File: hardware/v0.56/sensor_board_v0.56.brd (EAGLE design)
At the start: 50.8 x 50.8 mm, 65 parts, among them J3 USB-MICROB, U1 NEOPIXEL_NANO_2427, U10 TSL2591, U11 915MHz, U12 MH-Z19, U13 CCS811-I2C, U14 IAQ-CORE-C, U15 VLP-450-F, U16 VLP-450-F, U2 FT231XQ-R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

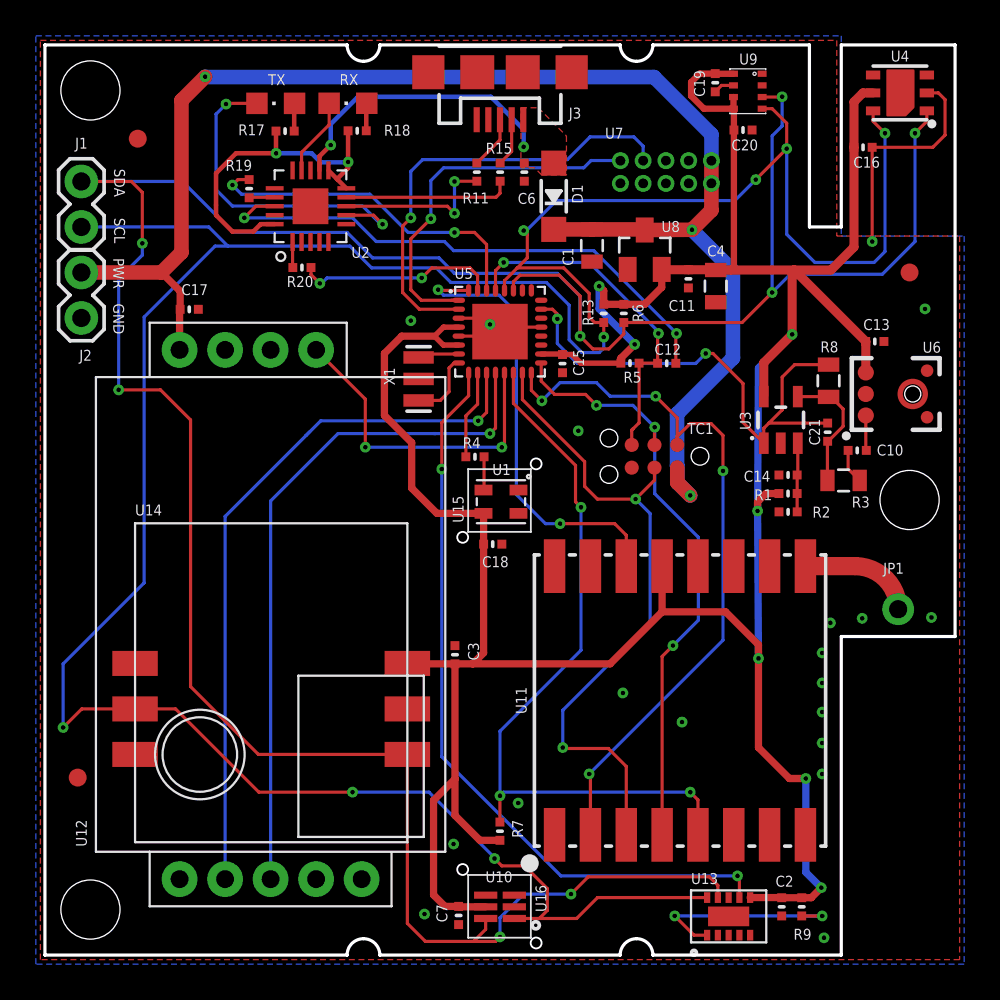
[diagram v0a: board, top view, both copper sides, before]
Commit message: Trace and silkscreen adjustments
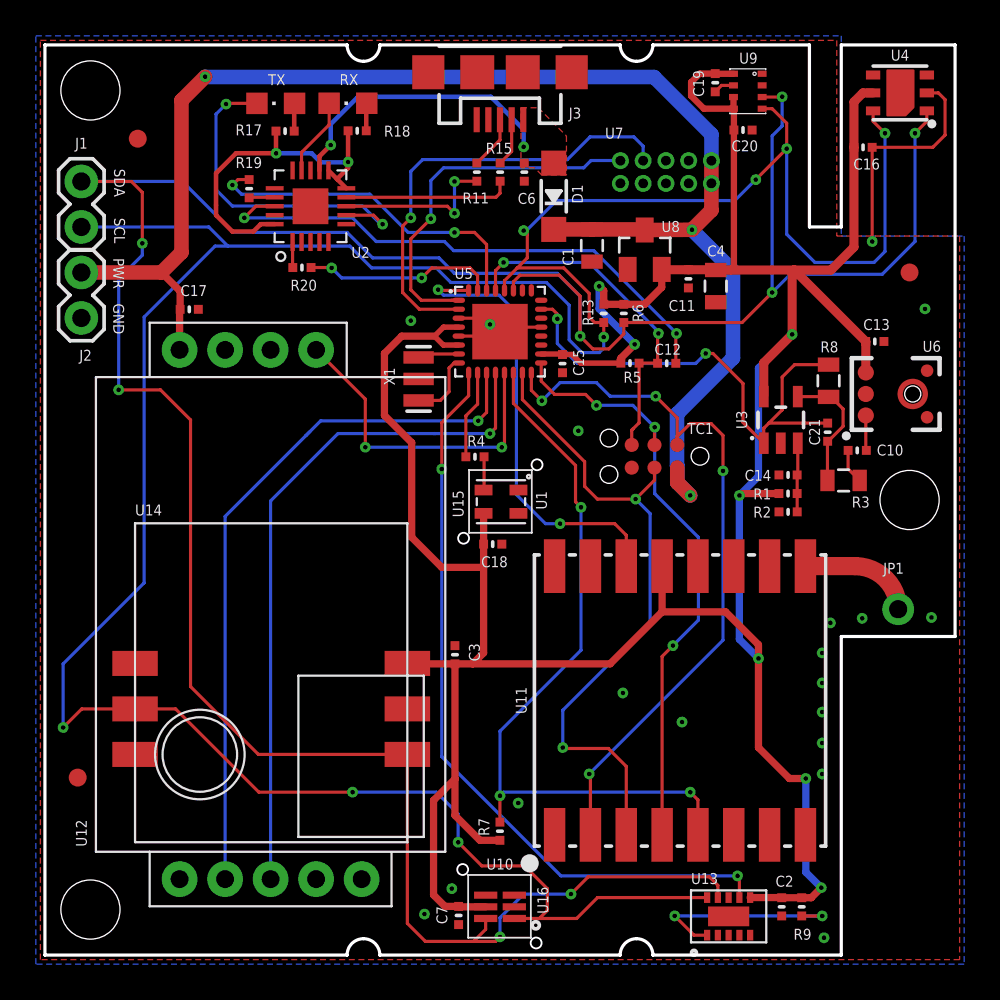
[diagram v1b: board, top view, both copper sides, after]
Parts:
- moved U15 0.07 mm to (23.4, 23.3)
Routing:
- net VCC: track 181.4 -> 185.5 mm
- net SCL: track 160.4 -> 161.4 mm
- net TX: track 11.3 -> 10.8 mm

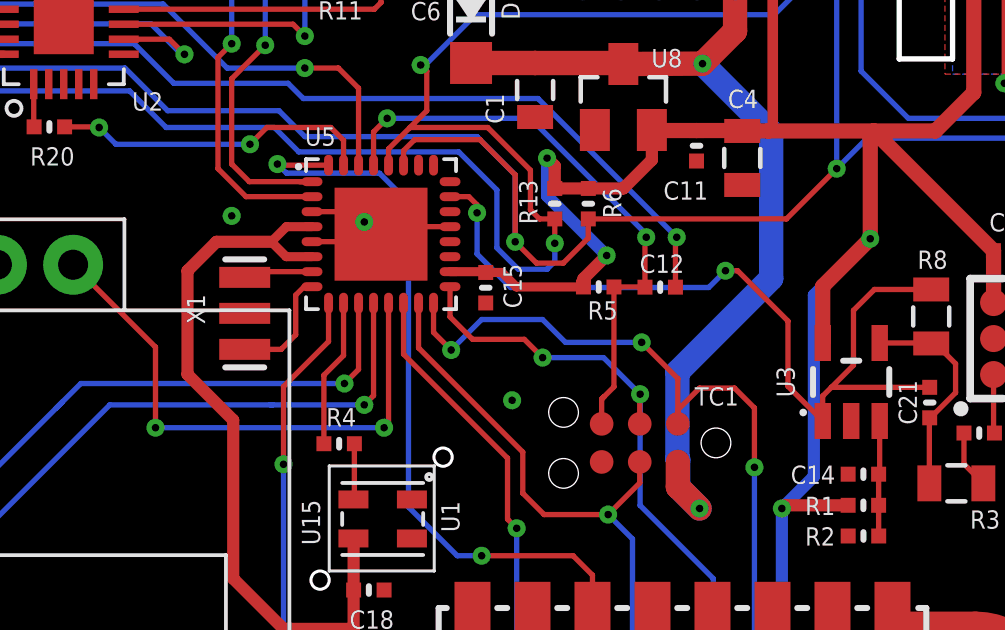
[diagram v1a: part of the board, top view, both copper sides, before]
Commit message: Added another decoupling cap to ATMega328P
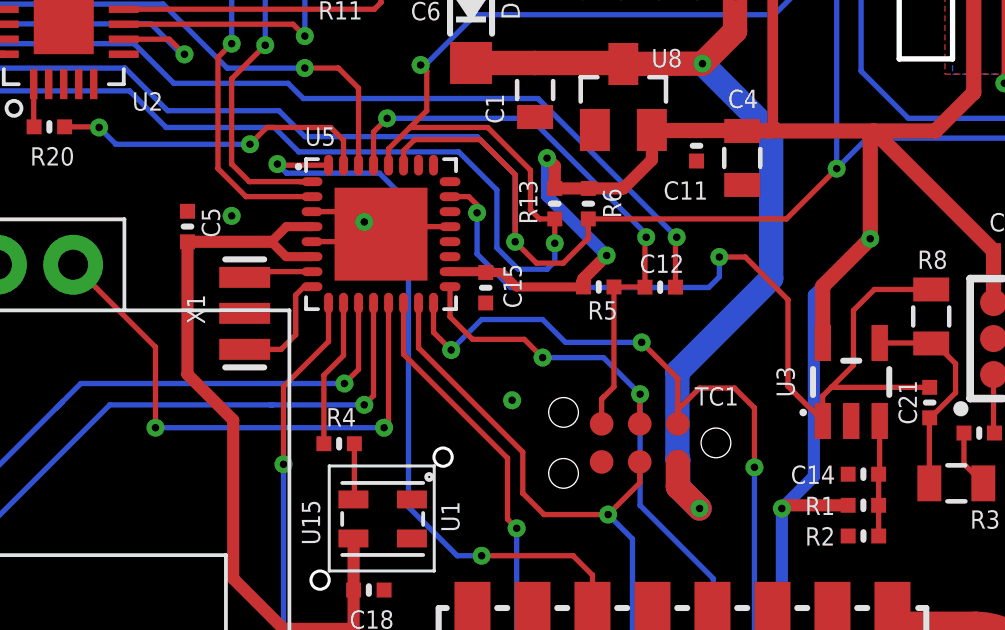
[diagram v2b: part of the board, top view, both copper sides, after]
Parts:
- added C5: 0.1uF, Adafruit Feather 32u4 Bluefruit LE:MICROBUILDER__0402MP
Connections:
- net GND: now also C5.1
- net VCC: now also C5.2
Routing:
- net A0: track 28.5 -> 29.7 mm
- net VCC: track 185.5 -> 186.1 mm
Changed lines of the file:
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@@
 <layer number="46" name="Milling" color="3" fill="1" visible="no" active="yes"/>
 <layer number="47" name="Measures" color="7" fill="1" visible="no" active="yes"/>
-<layer number="48" name="Document" color="7" fill="1" visible="no" active="yes"/>
-<layer number="49" name="Reference" color="7" fill="1" visible="no" active="yes"/>
+<layer number="48" name="Document" color="7" fill="1" visible="yes" active="yes"/>
+<layer number="49" name="Reference" color="7" fill="1" visible="yes" active="yes"/>
 <layer number="50" name="dxf" color="7" fill="1" visible="no" active="no"/>
 <layer number="51" name="tDocu" color="7" fill="1" visible="yes" active="yes"/>
@@
 <attribute name="NAME" x="27.4828" y="3.81" size="0.6096" layer="121" font="vector" rot="R270"/>
 </element>
+<element name="C5" library="Adafruit Feather 32u4 Bluefruit LE" package="MICROBUILDER__0402MP" value="0.1uF" x="18.9484" y="35.052" rot="R270"/>
 </elements>
 <signals>
@@
 <via x="43.3832" y="11.8364" extent="1-16" drill="0.25"/>
 <via x="49.1236" y="36.068" extent="1-16" drill="0.25"/>
+<contactref element="C5" pad="1"/>
 </signal>
 <signal name="VCC">
@@
 <wire x1="41.5544" y1="9.8552" x2="39.8272" y2="11.5824" width="0.4064" layer="1"/>
 <wire x1="39.8272" y1="11.5824" x2="39.8272" y2="16.5608" width="0.4064" layer="1"/>
-<wire x1="18.9484" y1="30.1244" x2="20.4724" y2="28.6004" width="0.4064" layer="1"/>
-<wire x1="18.9484" y1="30.1244" x2="18.9484" y2="33.5788" width="0.4064" layer="1"/>
-<wire x1="21.7424" y1="34.544" x2="19.9136" y2="34.544" width="0.4064" layer="1"/>
-<wire x1="18.9484" y1="33.5788" x2="19.9136" y2="34.544" width="0.4064" layer="1"/>
+<wire x1="20.4724" y1="28.6004" x2="18.9484" y2="30.1244" width="0.4064" layer="1"/>
 <wire x1="23.1" y1="35.048" x2="22.2464" y2="35.048" width="0.3048" layer="1"/>
 <wire x1="22.2464" y1="35.048" x2="21.7424" y2="34.544" width="0.3048" layer="1"/>
@@
 <wire x1="38.8662" y1="25.7598" x2="38.7604" y2="25.654" width="0.4064" layer="1"/>
 <wire x1="40.9696" y1="25.7598" x2="38.8662" y2="25.7598" width="0.4064" layer="1"/>
+<contactref element="C5" pad="2"/>
+<wire x1="18.95388125" y1="34.544" x2="18.9484" y2="34.544" width="0.4064" layer="1"/>
+<wire x1="18.95388125" y1="34.544" x2="21.7424" y2="34.544" width="0.4064" layer="1"/>
+<wire x1="18.9484" y1="34.53851875" x2="18.95388125" y2="34.544" width="0.4064" layer="1"/>
+<wire x1="18.9484" y1="30.1244" x2="18.9484" y2="34.53851875" width="0.4064" layer="1"/>
 <wire x1="24.4856" y1="22.9362" x2="24.4856" y2="21.6408" width="0" layer="19" extent="1-1"/>
 </signal>
@@
 <wire x1="28.3264" y1="36.048" x2="27.7" y2="36.048" width="0.1778" layer="1"/>
 <via x="28.6004" y="35.5092" extent="1-16" drill="0.25"/>
-<via x="36.8808" y="33.5788" extent="1-16" drill="0.25"/>
-<wire x1="38.9636" y1="31.9024" x2="38.9636" y2="29.7285" width="0.1778" layer="1"/>
-<wire x1="38.9636" y1="29.7285" x2="40.1218" y2="28.5703" width="0.1778" layer="1"/>
-<wire x1="37.2872" y1="33.5788" x2="36.8808" y2="33.5788" width="0.1778" layer="1"/>
-<wire x1="37.2872" y1="33.5788" x2="38.9636" y2="31.9024" width="0.1778" layer="1"/>
+<via x="36.6776" y="34.036" extent="1-16" drill="0.25"/>
+<wire x1="40.1218" y1="28.5703" x2="38.9636" y2="29.7285" width="0.1778" layer="1"/>
 <wire x1="43.688" y1="29.6926" x2="40.4114" y2="29.6926" width="0.1778" layer="1"/>
 <wire x1="40.1218" y1="28.5703" x2="40.1218" y2="29.403" width="0.1778" layer="1"/>
@@
 <wire x1="28.6004" y1="35.5092" x2="28.6004" y2="34.1376" width="0.1778" layer="16"/>
 <wire x1="28.6004" y1="34.1376" x2="29.718" y2="33.02" width="0.1778" layer="16"/>
-<wire x1="29.718" y1="33.02" x2="36.322" y2="33.02" width="0.1778" layer="16"/>
-<wire x1="36.322" y1="33.02" x2="36.8808" y2="33.5788" width="0.1778" layer="16"/>
+<wire x1="36.322" y1="33.02" x2="29.718" y2="33.02" width="0.1778" layer="16"/>
+<wire x1="36.6776" y1="34.036" x2="36.6776" y2="33.3756" width="0.1778" layer="16"/>
+<wire x1="36.6776" y1="33.3756" x2="36.322" y2="33.02" width="0.1778" layer="16"/>
+<wire x1="38.9636" y1="32.6136" x2="37.5412" y2="34.036" width="0.1778" layer="1"/>
+<wire x1="37.5412" y1="34.036" x2="36.6776" y2="34.036" width="0.1778" layer="1"/>
+<wire x1="38.9636" y1="29.7285" x2="38.9636" y2="32.6136" width="0.1778" layer="1"/>
 </signal>
 <signal name="DTR">

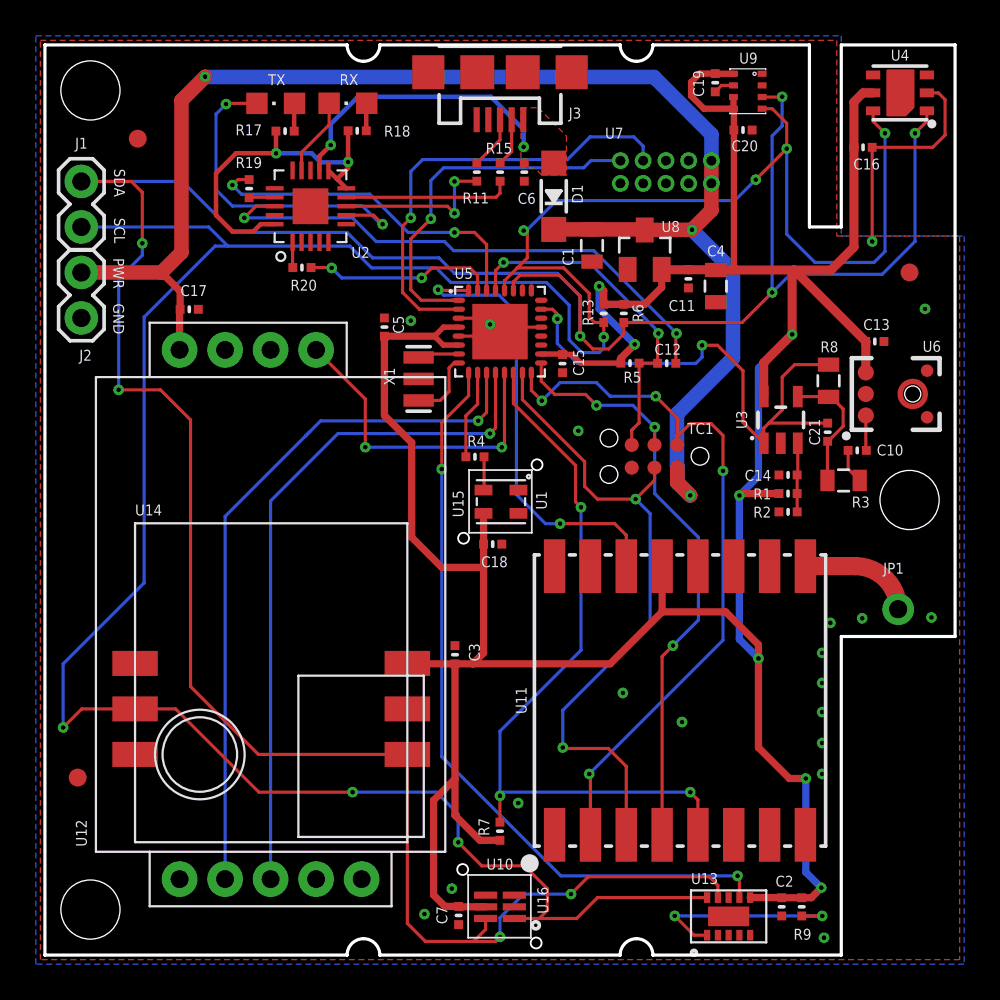
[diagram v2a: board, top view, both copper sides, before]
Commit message: v0.56b - minor adjustments
- Rerouted D9 trace to be SET pin for PM sensor instead of PWM pin for
CO2 sensor
- Added 10K pull up on D9
- Moved components away from light sensor and RGB LED's light pipe's
path
- Added extra vias all around for more ground stitching
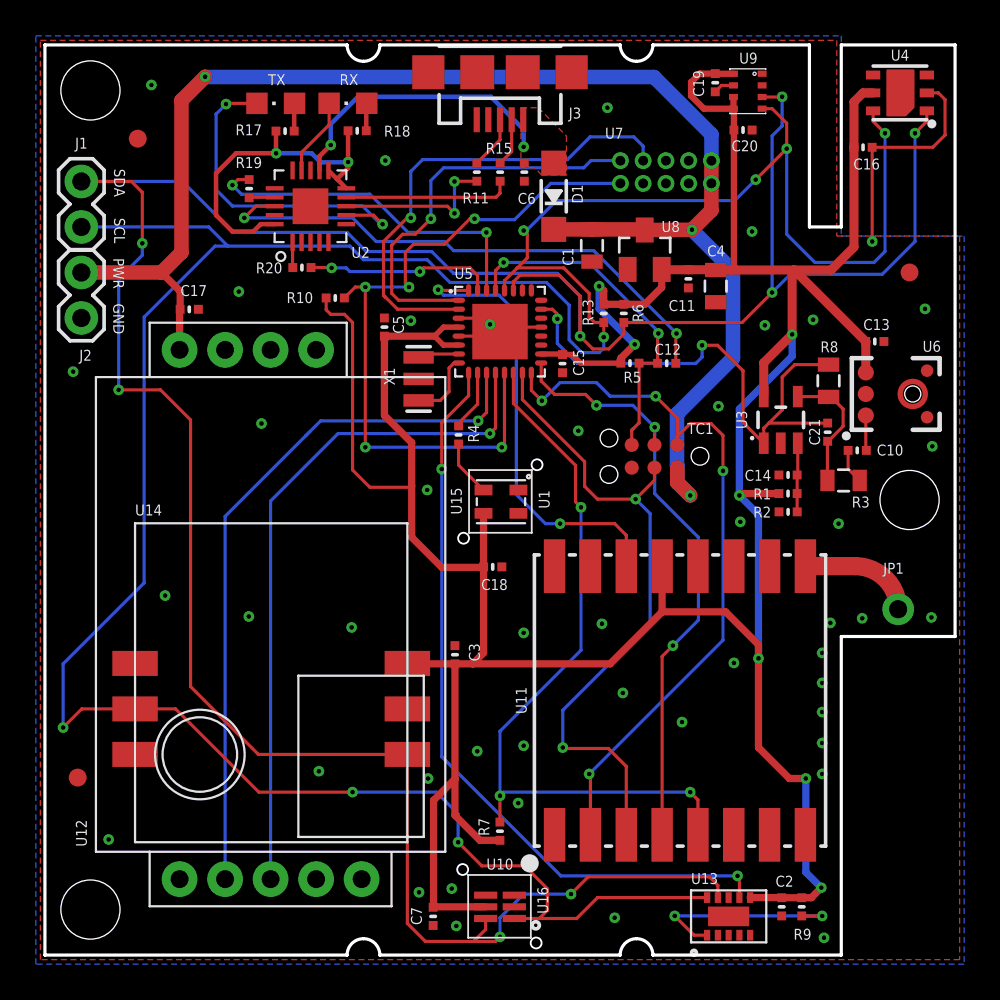
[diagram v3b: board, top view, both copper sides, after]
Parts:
- added R10: 10K, Adafruit Feather 32u4 Bluefruit LE:MICROBUILDER__0402MP
- moved R4 1.52 mm to (23.1, 29.0), turned to 270 degrees
- moved C7 1.42 mm to (21.7, 2.16)
- moved C18 1.27 mm to (25.0, 21.7)
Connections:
- net D9: now also R10.2, U7.10; no longer U12.PWM
- net VCC: now also R10.1
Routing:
- net D9: track 18.4 -> 40.3 mm, vias 2 -> 5
- net VCC: track 186.1 -> 200.9 mm
- net D3: track 20.9 -> 23.0 mm
- net D4: track 25.3 -> 27.1 mm
- net D6: track 4.96 -> 3.40 mm
- net N$1: track 1.87 -> 3.19 mm
- net GND: vias 19 -> 46
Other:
- board text added: "v0.56b | July 2017"
- board text removed: "v0.56 | June 2017"

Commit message: v0.56b - minor update
- Moved CO2 sensor up the board
- Updated library for light pipe
- Adjusted components around the light pipe
- Some silkscreen and trace adjustments
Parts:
- moved J2 5.08 mm to (2.03, 30.5)
- moved C17 2.62 mm to (7.65, 38.6)
- moved U12 2.57 mm to (2.44, 37.8)
- moved R10 1.22 mm to (17.4, 36.3)
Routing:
- net PWR: track 83.5 -> 86.3 mm
- net D7: track 39.8 -> 37.1 mm
- net D8: track 38.5 -> 36.1 mm
- net SCL: track 161.4 -> 163.7 mm
- net D9: track 40.3 -> 38.9 mm
- net VCC: track 200.9 -> 199.6 mm

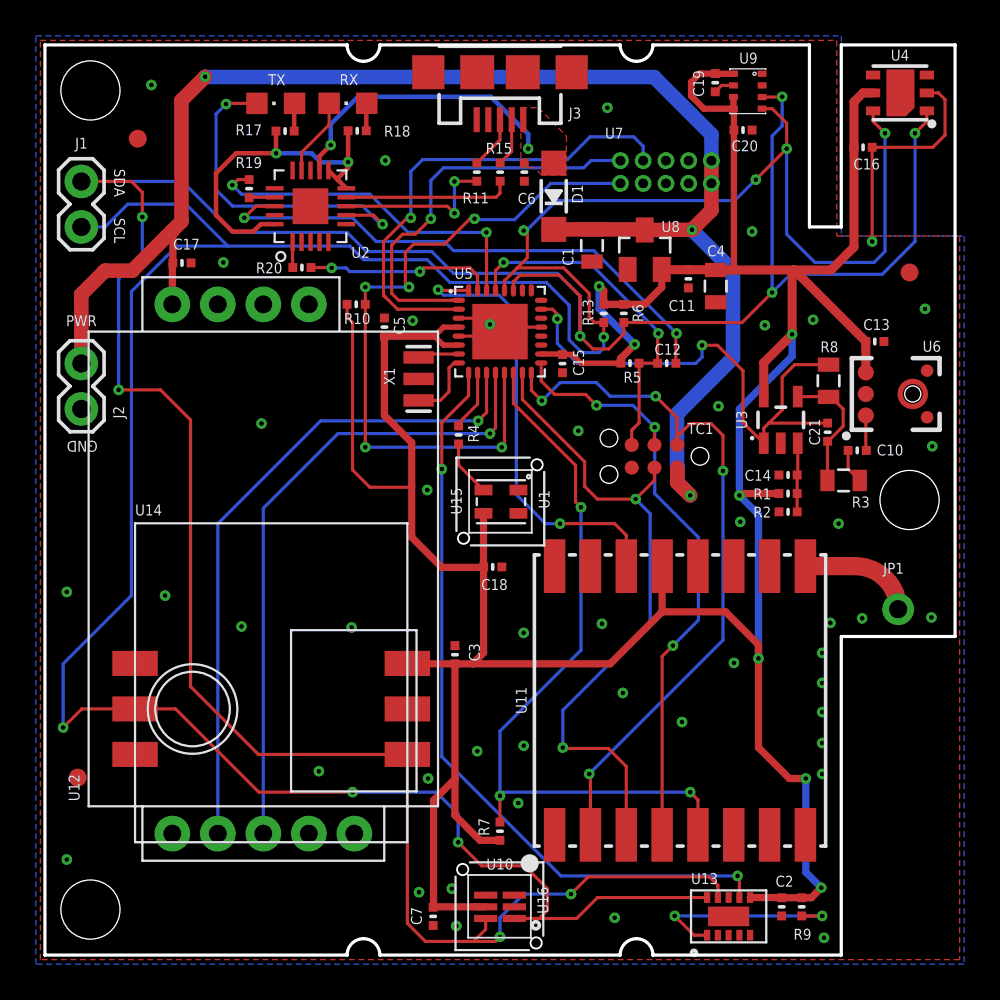
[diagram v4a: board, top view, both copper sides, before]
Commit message: Updated v0.56b with SMD pads for MH-z19 sensor
- other minor trace, parts and silkscreen adjustments
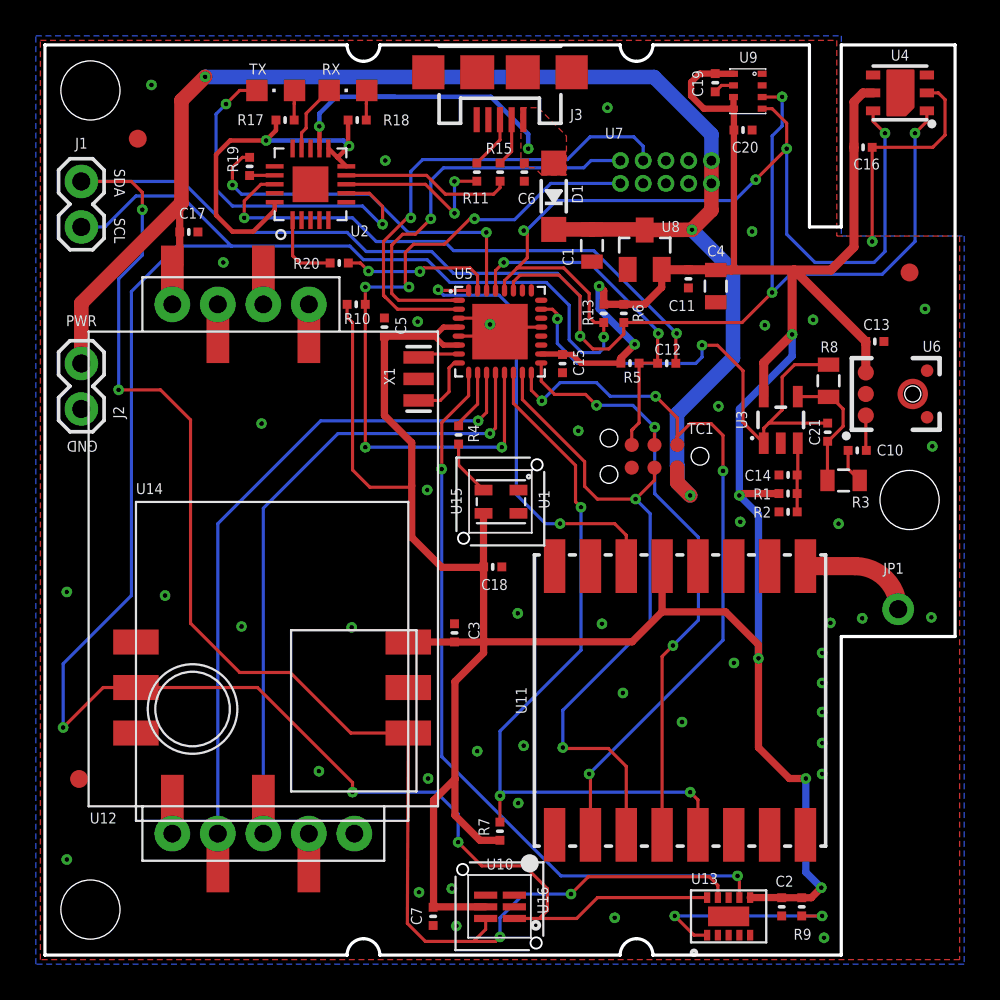
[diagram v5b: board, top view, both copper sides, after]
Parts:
- added U$4, U$5: 0878980426, 0878980426:CONN_4POS_VERT_2.54_SMD
- moved R20 2.10 mm to (16.4, 38.6)
- moved C17 1.77 mm to (8.03, 40.4)
- moved R19 1.24 mm to (11.4, 44.0)
- moved U2 1.22 mm to (14.8, 43.1)
- moved C3 1.22 mm to (22.9, 18.0)
- moved U14 1.19 mm to (5.08, 7.49)
- moved TX 0.72 mm to (12.9, 48.3)
- moved RX 0.72 mm to (16.9, 48.3)
- moved R17 0.62 mm to (13.4, 46.6)
- moved R18 0.60 mm to (17.4, 46.6)
- moved U$2 0.11 mm to (1.91, 9.83)
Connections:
- new net N$12: U$4.P$4
- new net N$14: U$5.P$1
- new net N$19: U$5.P$4
- new net N$8: U$4.P$3
- net D7: now also U$5.P$2
- net D8: now also U$5.P$3
- net GND: now also U$4.P$2
- net PWR: now also U$4.P$1
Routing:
- net N$2: track 1.43 -> 4.25 mm
- net TX: track 10.5 -> 8.50 mm
- net SCL: track 163.7 -> 165.6 mm
- net D8: track 36.1 -> 37.9 mm
- net D7: track 37.1 -> 38.9 mm
- net VBUS: track 16.2 -> 17.8 mm
- net N$18: track 19.1 -> 20.5 mm
- net SDA: track 161.7 -> 160.4 mm
- net FTDI_VCC: track 19.8 -> 21.0 mm
- net RX: track 19.6 -> 20.7 mm
- net DTR: track 30.5 -> 31.5 mm
- net PWR: track 86.3 -> 87.1 mm
- net N$17: track 4.39 -> 3.88 mm
- net N$26: track 9.23 -> 9.74 mm
